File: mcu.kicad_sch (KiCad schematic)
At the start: 21 parts, among them J301 GPIO, SW301 RST, SW302 BOOT0, U301 STM32G0B1KBUx

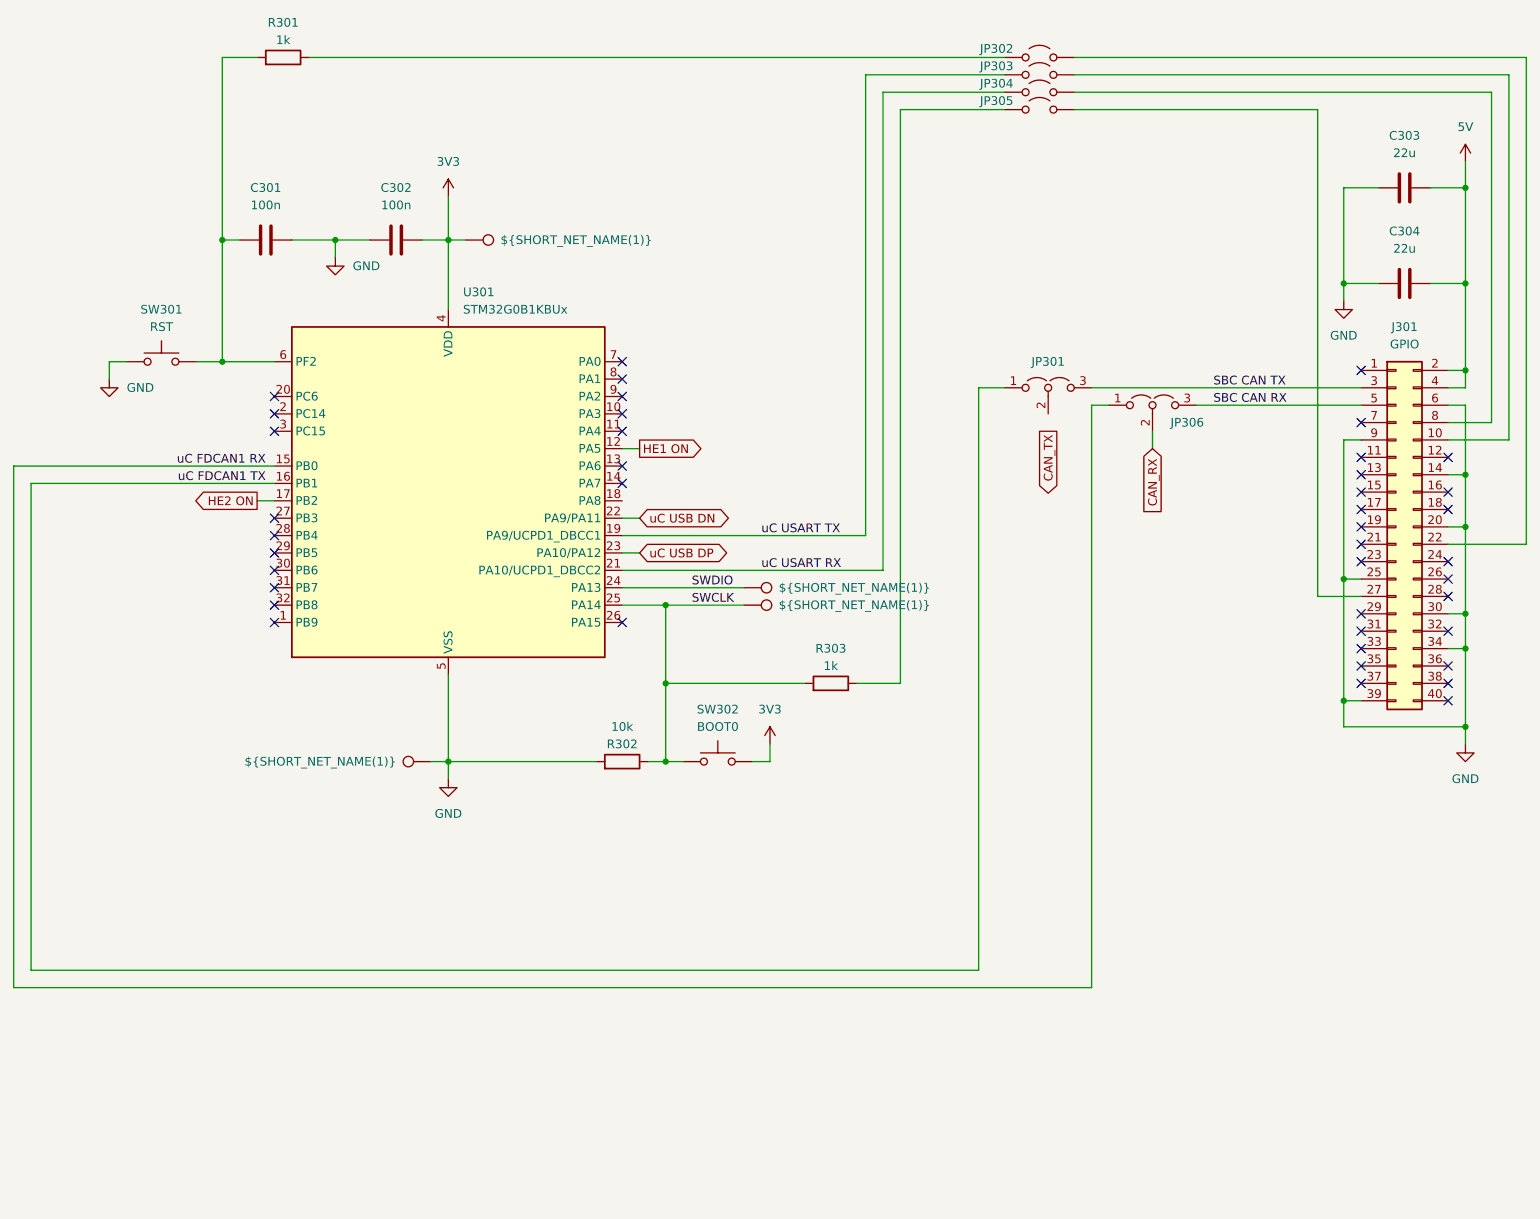
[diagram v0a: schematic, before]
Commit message: Rev 0.2: Major hardware improvements and production readiness
Hardware Improvements (Thanks to shx for schematic cleanup):
- Clean up schematic organization and structure
- Set CAN transceiver Silent pin to GND for stability
- Add status LEDs (yellow: 24V/5V/3.3V, green: MCU PB4)
- Replace jumpers with solder jumpers on bottom side
- Add jumpers to output PFETs for permanent-on without firmware
- Add robust test points for 5V/GND load testing
- Add optional heatsink for DC/DC converter on bottom
- Add 10µF capacitor for MCU on 3.3V rail

Component Optimizations:
- Replace 30kΩ with 33kΩ basic part for simplified BOM
- Change DC/DC feedback: 15.5kΩ15kΩ (new output: 5.1V)
- Upgrade CAN ESD protection: NUP2105LPESD1CAN
- Increase CAN termination resistor footprint: 04020603
- Switch USB hub supply from 5V to 3.3V per datasheet

Production Ready:
- Add all LCSC part numbers and rotations
- Generate complete production data package
- Improve PCB layout and button placement
- Create comprehensive changelog documentation
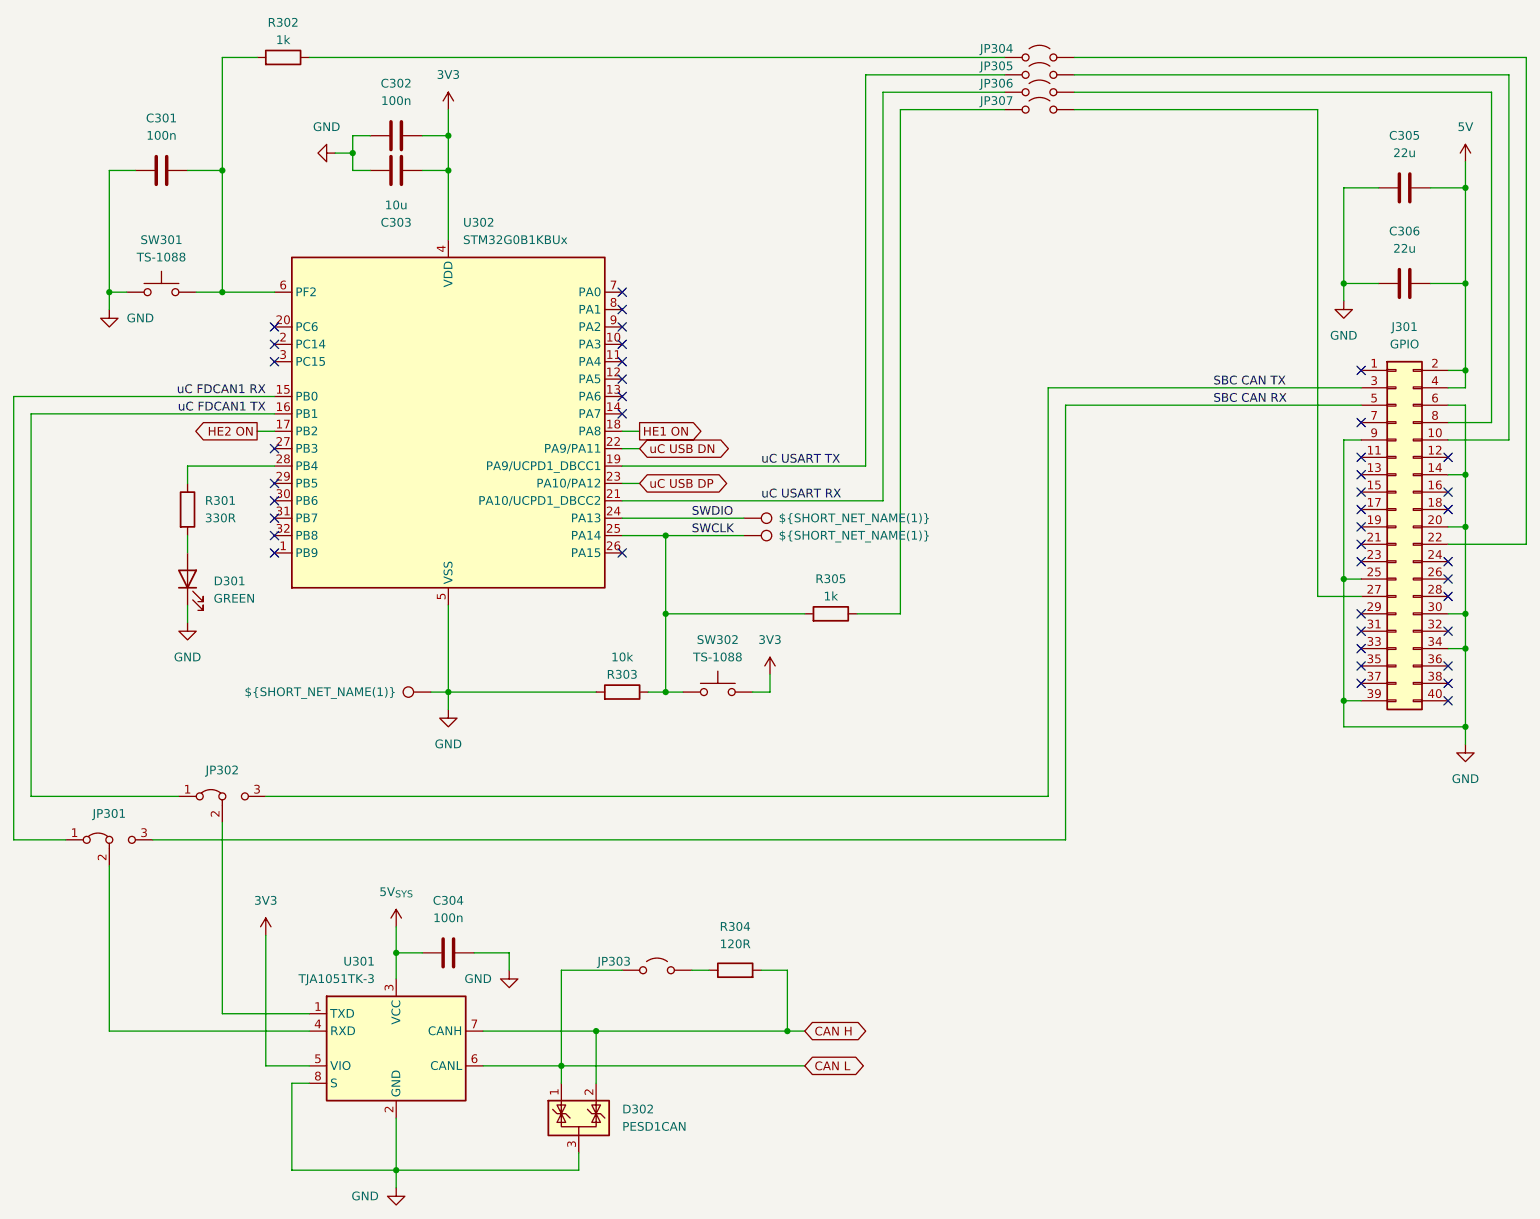
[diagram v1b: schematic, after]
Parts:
- removed TP302: ${SHORT_NET_NAME(1)}, project:NAMED_TEST_POINT, symbol project:NamedTestPoint
- added C303: 10u, Capacitor_SMD:C_0603_1608Metric, symbol Device:C
- added C304: 100n, Capacitor_SMD:C_0402_1005Metric, symbol Device:C
- added D301: GREEN, LED_SMD:LED_0805_2012Metric, symbol Device:LED
- added D302: PESD1CAN, Package_TO_SOT_SMD:SOT-23, symbol Power_Protection:NUP2105L
- added JP303: ~, Jumper:SolderJumper-2_P1.3mm_Open_RoundedPad1.0x1.5mm, symbol Jumper:Jumper_2_Open
- added R301: 330R, Resistor_SMD:R_0402_1005Metric, symbol Device:R
- added R304: 120R, Resistor_SMD:R_0603_1608Metric, symbol Device:R
- added U301: TJA1051TK-3, Package_SON:HVSON-8-1EP_3x3mm_P0.65mm_EP1.6x2.4mm, symbol Interface_CAN_LIN:TJA1051TK-3
- C301, C302: LCSC Part # (none) -> C307331; Manufacturer Part # (none) -> CL05B104KB54PNC
- C305: renamed from C303; LCSC Part # (none) -> C12891; Manufacturer Part # (none) -> CL31A226KAHNNNE
- C306: renamed from C304; LCSC Part # (none) -> C12891; Manufacturer Part # (none) -> CL31A226KAHNNNE
- JP301: renamed from JP306; value Jumper_3_Open -> ~; footprint Connector_PinHeader_2.54mm:PinHeader_1x03_P2.54mm_Vertical -> project:SolderJumper-3_P1.3mm_Bridged12_RoundedPad1.0x1.5mm_custom; symbol Jumper:Jumper_3_Open -> Jumper:Jumper_3_Bridged12
- JP302: renamed from JP301; value Jumper_3_Open -> ~; footprint Connector_PinHeader_2.54mm:PinHeader_1x03_P2.54mm_Vertical -> project:SolderJumper-3_P1.3mm_Bridged12_RoundedPad1.0x1.5mm_custom; symbol Jumper:Jumper_3_Open -> Jumper:Jumper_3_Bridged12
- JP304: renamed from JP302; footprint Connector_PinHeader_2.54mm:PinHeader_1x02_P2.54mm_Vertical -> Jumper:SolderJumper-2_P1.3mm_Open_RoundedPad1.0x1.5mm; now left out of the parts list
- JP305: renamed from JP303; footprint Connector_PinHeader_2.54mm:PinHeader_1x02_P2.54mm_Vertical -> Jumper:SolderJumper-2_P1.3mm_Open_RoundedPad1.0x1.5mm; now left out of the parts list
- JP306: renamed from JP304; footprint Connector_PinHeader_2.54mm:PinHeader_1x02_P2.54mm_Vertical -> Jumper:SolderJumper-2_P1.3mm_Open_RoundedPad1.0x1.5mm; now left out of the parts list
- JP307: renamed from JP305; footprint Connector_PinHeader_2.54mm:PinHeader_1x02_P2.54mm_Vertical -> Jumper:SolderJumper-2_P1.3mm_Open_RoundedPad1.0x1.5mm; now left out of the parts list
- R302: renamed from R301; LCSC Part # (none) -> C11702; Manufacturer Part # (none) -> 0402WGF1001TCE
- R303: renamed from R302; LCSC Part # (none) -> C25744; Manufacturer Part # (none) -> 0402WGF1002TCE
- R305: renamed from R303; LCSC Part # (none) -> C11702; Manufacturer Part # (none) -> 0402WGF1001TCE
- SW301: value RST -> TS-1088; LCSC Part # (none) -> C720477; Manufacturer Part # (none) -> TS-1088-AR02016
- SW302: value BOOT0 -> TS-1088; LCSC Part # (none) -> C720477; Manufacturer Part # (none) -> TS-1088-AR02016
- TP301: now left out of the parts list
- TP302: renamed from TP303; now left out of the parts list
- TP303: renamed from TP304; now left out of the parts list
- U302: renamed from U301; FT Rotation Offset (none) -> 270; LCSC Part # (none) -> C5159549; Manufacturer Part # (none) -> STM32G0B1KBU6
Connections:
- net 3V3: now also C303.1, U301.5 (VIO)
- net GND: now also C303.2, C304.1, D301.1 (K), D302.3 (A), U301.2 (GND), U301.8 (S), U301.9 (GND)
- net HE1 ON: now also U302.18 (PA8); no longer U302.12 (PA5)
- net at U302.28 (PB4): now also R301.1
- net at JP302.2 (C): now also U301.1 (TXD)
- net CAN_RX: no longer names the net of JP301.2 (C)
- net CAN_RX: now also U301.4 (RXD)
- new net: D301.2 (A), R301.2
- new net: JP303.2 (B), R304.1
- new net 5V_{SYS}: C304.2, U301.3 (VCC)
- new net CAN H: D302.2 (K), R304.2, U301.7 (CANH)
- new net CAN L: D302.1 (K), JP303.1 (A), U301.6 (CANL)
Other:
- moved on the sheet: C301, C302, R303, R305, SW301, SW302, U302
